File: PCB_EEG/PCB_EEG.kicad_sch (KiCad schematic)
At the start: 1 part

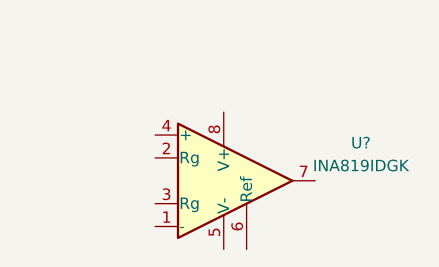
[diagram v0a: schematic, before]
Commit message: updated symbol library
added symbol & footprint for instrumentation opamp - INA819ID

removed old component
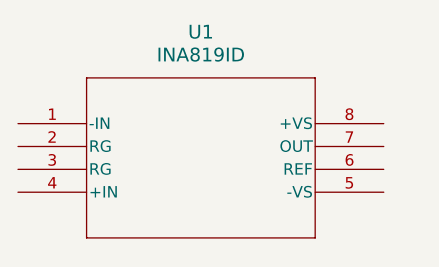
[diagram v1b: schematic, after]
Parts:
- removed U?: INA819IDGK, Package_SO:VSSOP-8_3.0x3.0mm_P0.65mm, symbol EEG part lib:INA819IDGK
- added U1: INA819ID, EEG Footprints:INA819ID, symbol EEG_Part_Library:INA819ID
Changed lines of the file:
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@@
 (kicad_sch (version 20230121) (generator eeschema)
   (paper "A4")
-  (symbol (lib_id "EEG part lib:INA819IDGK") (at 92.71 67.31 0) (unit 1)
+  (symbol (lib_id "EEG_Part_Library:INA819ID") (at 69.85 60.96 0) (unit 1)
     (in_bom yes) (on_board yes) (dnp no) (fields_autoplaced)
-    (property "Reference" "U?" (at 107.95 63.1191 0)
-      (effects (font (size 1.27 1.27)))
+    (property "Reference" "U1" (at 90.17 50.8 0)
+      (effects (font (size 1.524 1.524)))
     )
-    (property "Value" "INA819IDGK" (at 107.95 65.6591 0)
-      (effects (font (size 1.27 1.27)))
+    (property "Value" "INA819ID" (at 90.17 53.34 0)
+      (effects (font (size 1.524 1.524)))
     )
-    (property "Footprint" "Package_SO:VSSOP-8_3.0x3.0mm_P0.65mm" (at 92.71 88.9 0)
-      (effects (font (size 1.27 1.27)) hide)
+    (property "Footprint" "EEG Footprints:INA819ID" (at 69.85 60.96 0)
+      (effects (font (size 1.27 1.27) italic) hide)
     )
-    (property "Datasheet" "https://www.ti.com/lit/ds/symlink/ina819.pdf" (at 92.71 86.36 0)
-      (effects (font (size 1.27 1.27)) hide)
+    (property "Datasheet" "INA819ID" (at 69.85 60.96 0)
+      (effects (font (size 1.27 1.27) italic) hide)
     )
     (pin "1")
@@
       (project "PCB_EEG"
         (path "/b1f30c8e-e9f4-4a87-bf16-63bb5eae0007"
-          (reference "U?") (unit 1)
+          (reference "U1") (unit 1)
         )
       )
